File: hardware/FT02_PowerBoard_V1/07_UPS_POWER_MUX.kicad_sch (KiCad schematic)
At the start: 0 parts

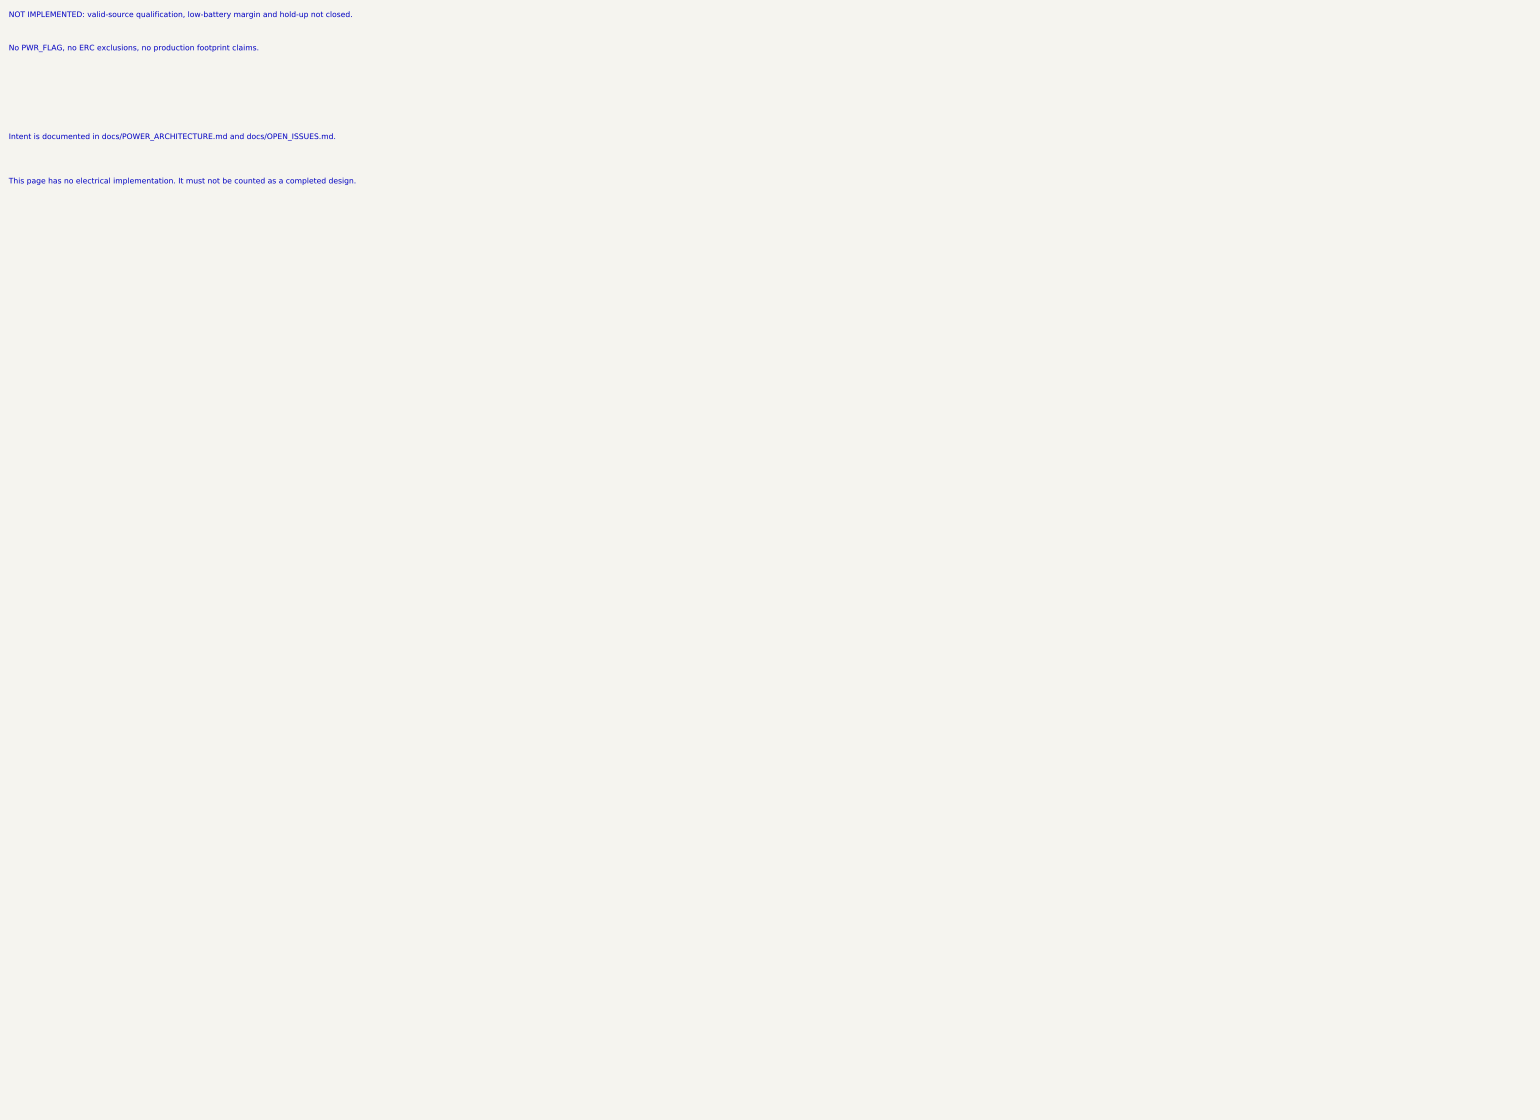
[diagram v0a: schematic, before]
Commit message: Wire FT02 Phase 1 power stages and verify partial shunt boundary
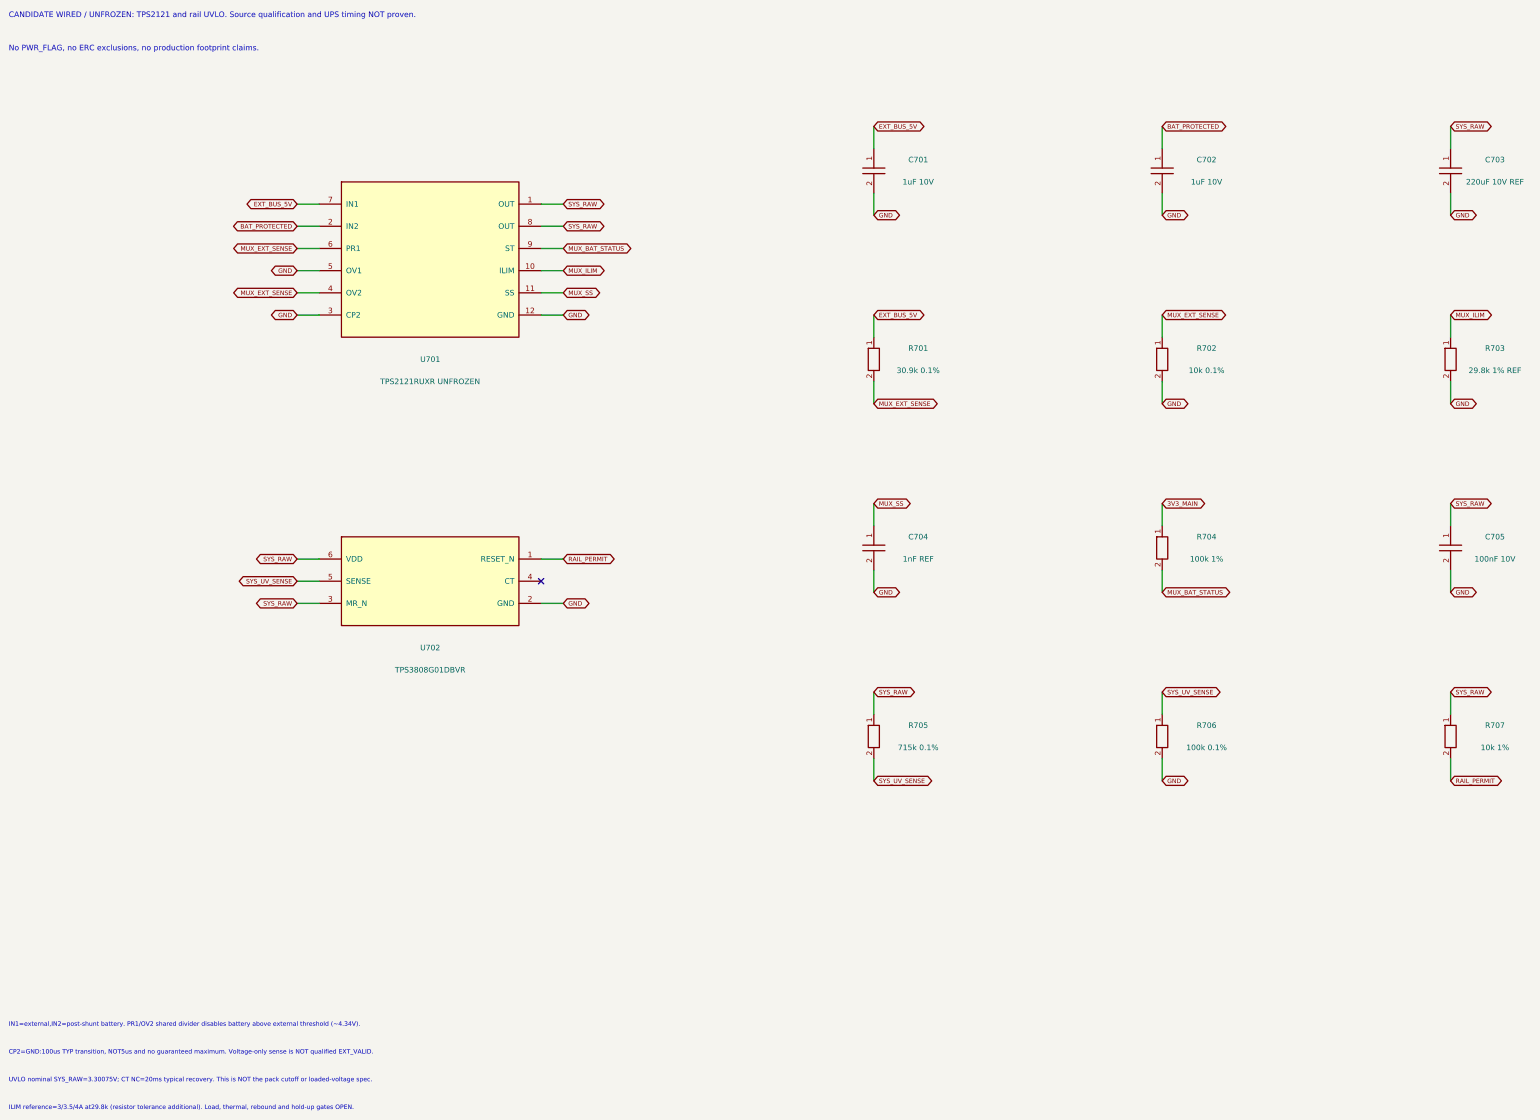
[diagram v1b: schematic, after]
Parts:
- added C701, C702: 1uF 10V, symbol FT02_Reference:C
- added C703: 220uF 10V REF, symbol FT02_Reference:C
- added C704: 1nF REF, symbol FT02_Reference:C
- added C705: 100nF 10V, symbol FT02_Reference:C
- added R701: 30.9k 0.1%, symbol FT02_Reference:R
- added R702: 10k 0.1%, symbol FT02_Reference:R
- added R703: 29.8k 1% REF, symbol FT02_Reference:R
- added R704: 100k 1%, symbol FT02_Reference:R
- added R705: 715k 0.1%, symbol FT02_Reference:R
- added R706: 100k 0.1%, symbol FT02_Reference:R
- added R707: 10k 1%, symbol FT02_Reference:R
- added U701: TPS2121RUXR UNFROZEN, symbol FT02_Reference:TPS2121
- added U702: TPS3808G01DBVR, symbol FT02_Reference:TPS3808G01DBV
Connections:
- new net 3V3_MAIN: R704.1
- new net BAT_PROTECTED: C702.1, U701.2 (IN2)
- new net EXT_BUS_5V: C701.1, R701.1, U701.7 (IN1)
- new net GND: C701.2, C702.2, C703.2, C704.2, C705.2, R702.2, R703.2, R706.2, U701.12 (GND), U701.3 (CP2), U701.5 (OV1), U702.2 (GND)
- new net MUX_BAT_STATUS: R704.2, U701.9 (ST)
- new net MUX_EXT_SENSE: R701.2, R702.1, U701.4 (OV2), U701.6 (PR1)
- new net MUX_ILIM: R703.1, U701.10 (ILIM)
- new net MUX_SS: C704.1, U701.11 (SS)
- new net RAIL_PERMIT: R707.2, U702.1 (RESET_N)
- new net SYS_RAW: C703.1, C705.1, R705.1, R707.1, U701.1 (OUT), U701.8 (OUT), U702.3 (MR_N), U702.6 (VDD)
- new net SYS_UV_SENSE: R705.2, R706.1, U702.5 (SENSE)
- no-connect marks 0 -> 1
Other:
- note added: "CANDIDATE WIRED / UNFROZEN: TPS2121 and rail UVLO. Source qualification and UPS timing NOT proven."
- note added: "CP2=GND:100us TYP transition, NOT5us and no guaranteed maximum. Voltage-only sense is NOT qualified EXT_VALID."
- note added: "ILIM reference=3/3.5/4A at29.8k (resistor tolerance additional). Load, thermal, rebound and hold-up gates OPEN."
- note added: "IN1=external,IN2=post-shunt battery. PR1/OV2 shared divider disables battery above external threshold (~4.34V)."
- note added: "UVLO nominal SYS_RAW=3.30075V; CT NC=20ms typical recovery. This is NOT the pack cutoff or loaded-voltage spec."
- note removed: "Intent is documented in docs/POWER_ARCHITECTURE.md and docs/OPEN_ISSUES.md."
- note removed: "NOT IMPLEMENTED: valid-source qualification, low-battery margin and hold-up not closed."
- note removed: "This page has no electrical implementation. It must not be counted as a completed design."

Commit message: Wire FT02 mechanical master power gate and audit load unknowns
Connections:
- net SYS_RAW: no longer C703.1, U701.1 (OUT), U701.8 (OUT)
- new net UPS_RAW: C703.1, U701.1 (OUT), U701.8 (OUT)
